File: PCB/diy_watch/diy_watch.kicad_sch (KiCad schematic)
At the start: 45 parts, among them J1 USB_B_Micro, SW1 SW_Push, U1 W25Q32JVSS, U2 DS3231MZ, U3 RP2040, U5 LTC4054ES5-4.2, U7 XC6210B332MR, Y1 12MHz_crystal

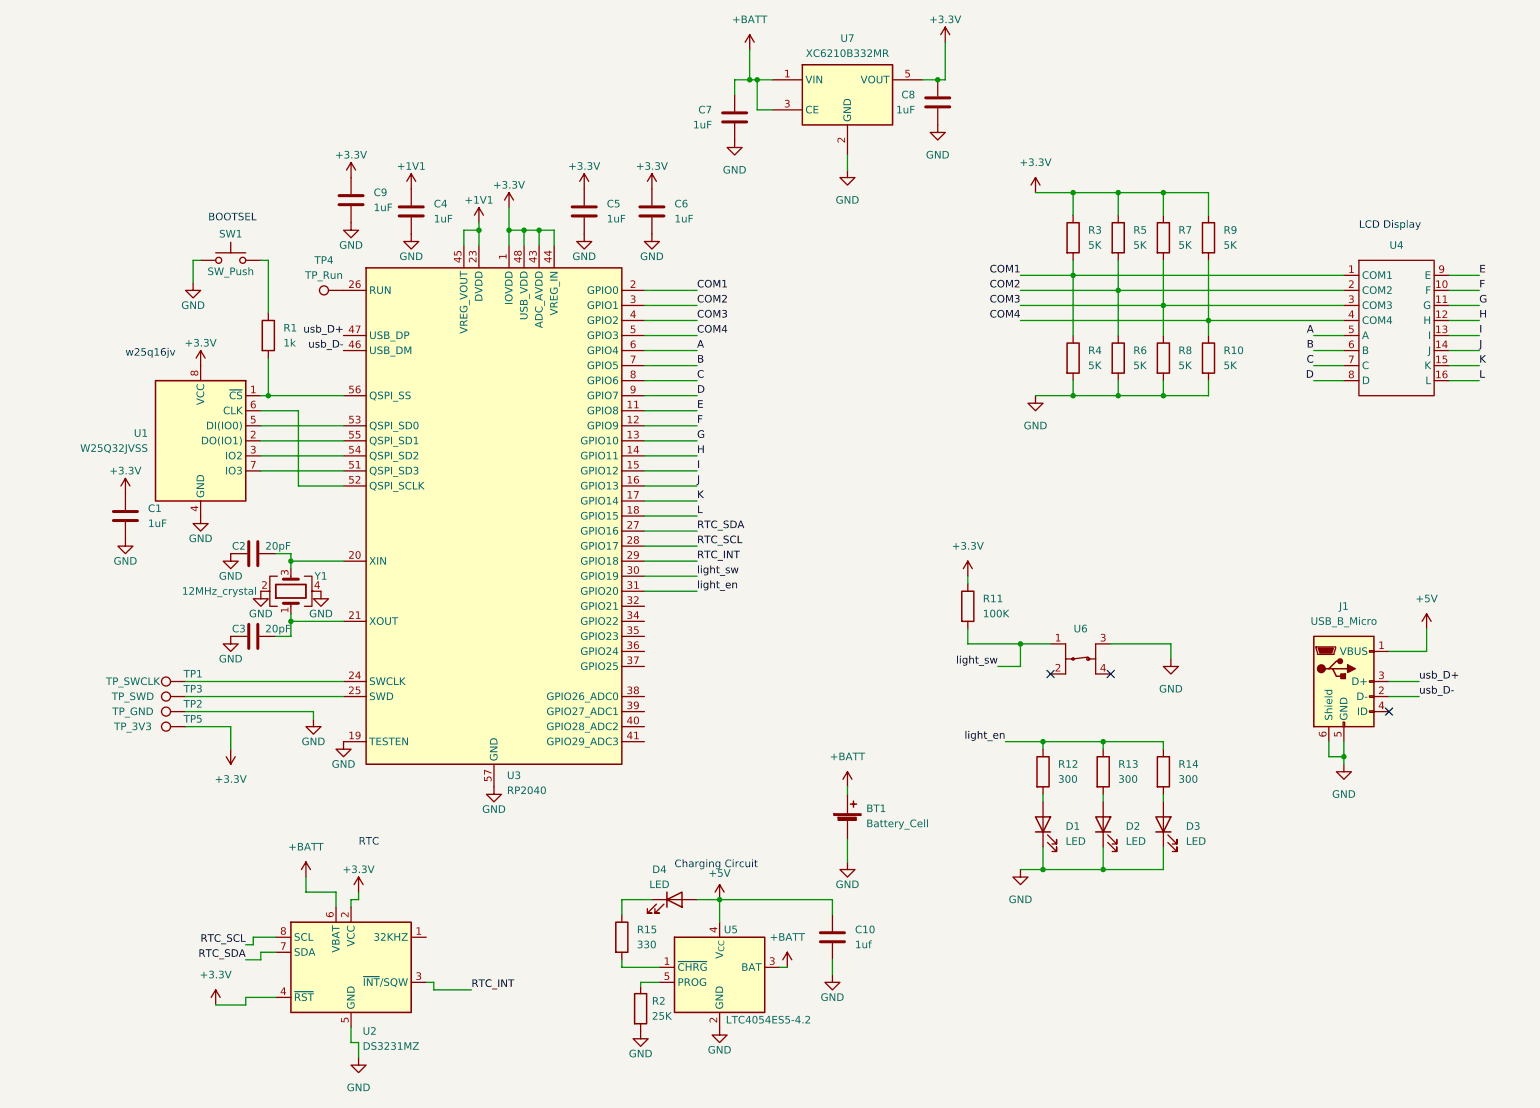
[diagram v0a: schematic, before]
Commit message: Changed charging chip and flash chip, rearranged parts
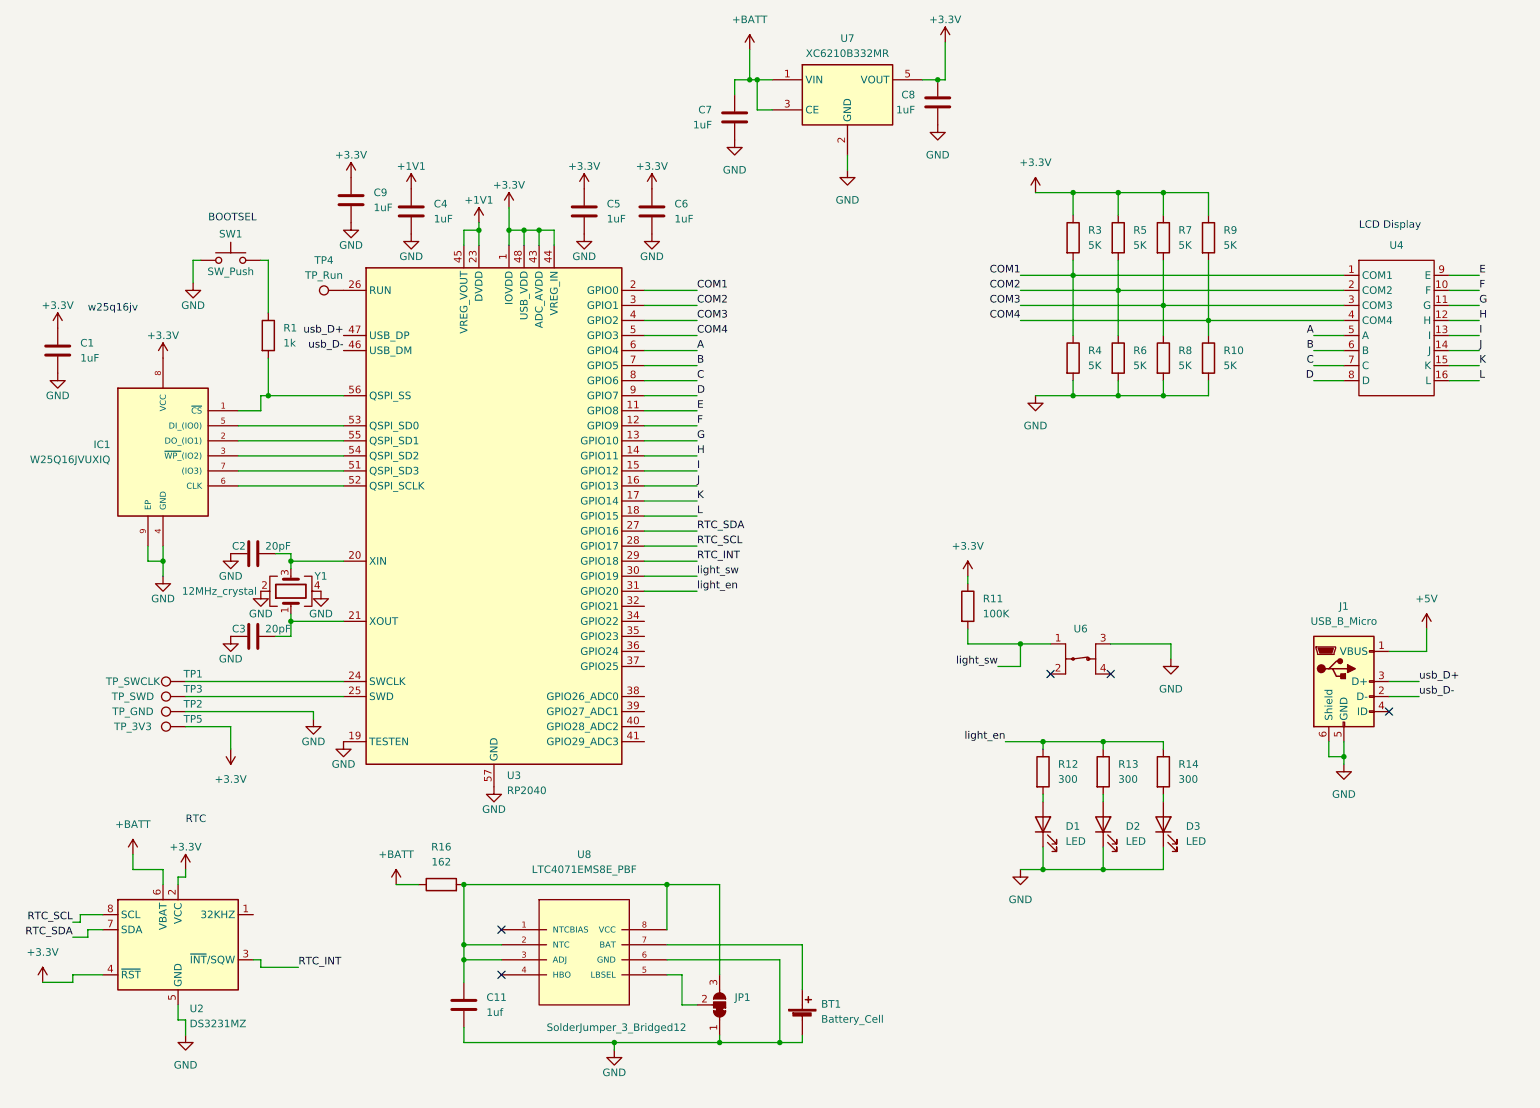
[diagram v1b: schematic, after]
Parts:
- removed C10: 1uf, Capacitor_SMD:C_0402_1005Metric, symbol Device:C
- removed D4: LED, LED_SMD:LED_0805_2012Metric_Pad1.15x1.40mm_HandSolder, symbol Device:LED
- removed R15: 330, Resistor_SMD:R_0805_2012Metric_Pad1.20x1.40mm_HandSolder, symbol Device:R
- removed R2: 25K, Resistor_SMD:R_0402_1005Metric, symbol Device:R
- removed U1: W25Q32JVSS, Package_SO:SOIC-8_3.9x4.9mm_P1.27mm, symbol Memory_Flash:W25Q32JVSS
- removed U5: LTC4054ES5-4.2, Package_TO_SOT_SMD:TSOT-23-5, symbol Battery_Management:LTC4054ES5-4.2
- added C11: 1uf, Capacitor_SMD:C_0402_1005Metric, symbol Device:C
- added IC1: W25Q16JVUXIQ, DIY_Watch_lib:SON50P300X200X60-9N, symbol DIY_Watch_lib:W25Q16JVUXIQ
- added JP1: SolderJumper_3_Bridged12, Jumper:SolderJumper-3_P1.3mm_Bridged12_Pad1.0x1.5mm, symbol Jumper:SolderJumper_3_Bridged12
- added R16: 162, Resistor_SMD:R_0402_1005Metric, symbol Device:R
- added U8: LTC4071EMS8E_PBF, Package_SO:MSOP-8-1EP_3x3mm_P0.65mm_EP1.5x1.8mm_ThermalVias, symbol DIY_Watch_lib:LTC4071EMS8E_PBF
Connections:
- net +3.3V: now also IC1.8 (VCC)
- net +BATT: now also R16.1; no longer BT1.1 (+)
- net GND: now also C11.2, IC1.4 (GND), IC1.9 (EP), JP1.1 (A), U8.6 (GND)
- net at R1.2, U3.56 (QSPI_SS): now also IC1.1 (~{CS})
- net at U3.55 (QSPI_SD1): now also IC1.2 (DO_(IO1))
- net at U3.54 (QSPI_SD2): now also IC1.3 (~{WP_}(IO2))
- net at U3.53 (QSPI_SD0): now also IC1.5 (DI_(IO0))
- net at U3.52 (QSPI_SCLK): now also IC1.6 (CLK)
- net at U3.51 (QSPI_SD3): now also IC1.7 ((IO3))
- new net: C11.1, JP1.3 (B), R16.2, U8.2 (NTC), U8.3 (ADJ), U8.8 (VCC)
- new net: JP1.2 (C), U8.5 (LBSEL)
- new net: BT1.1 (+), U8.7 (BAT)
- no-connect marks 3 -> 5
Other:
- note removed: "Charging Circuit"
- moved on the sheet: BT1, C1, U2

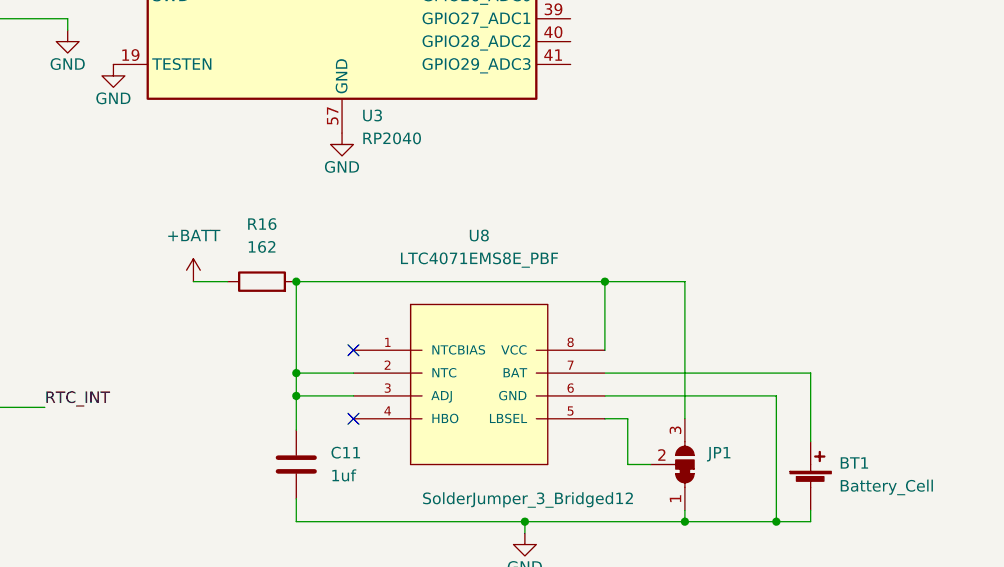
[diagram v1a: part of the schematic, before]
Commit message: Re-routed refactored board
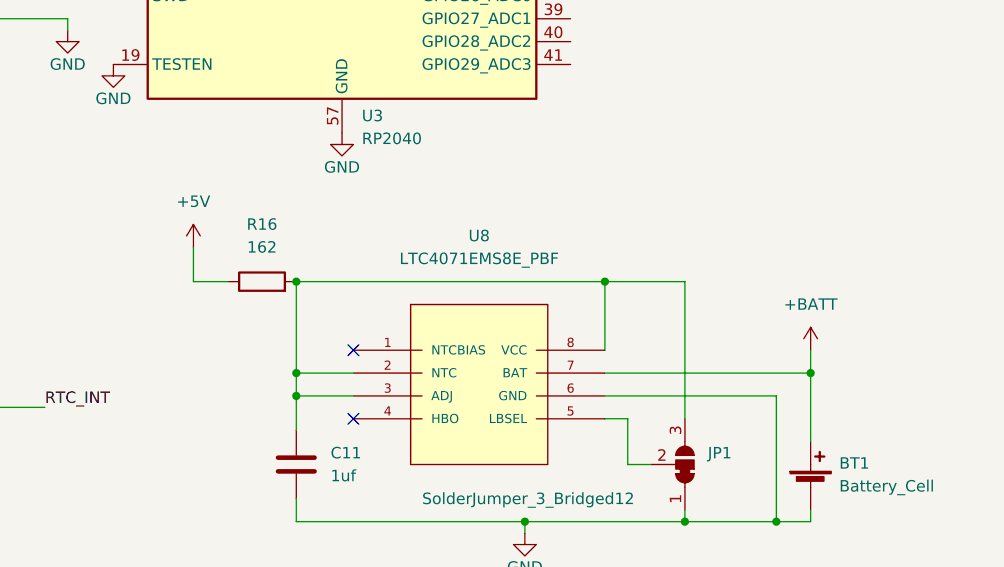
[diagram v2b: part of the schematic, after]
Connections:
- net +5V: now also R16.1
- net +BATT: now also BT1.1 (+), U8.7 (BAT); no longer R16.1
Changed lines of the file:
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@@
   (junction (at 195.58 158.75) (diameter 0) (color 0 0 0 0)
   )
+  (junction (at 154.94 171.45) (diameter 0) (color 0 0 0 0)
+  )
   (no_connect (at 207.01 125.73))
   (no_connect (at 104.14 168.91))
@@
     (stroke (width 0) (type default))
   )
-  (wire (pts (xy 154.94 171.45) (xy 154.94 179.07))
+  (wire (pts (xy 154.94 168.91) (xy 154.94 171.45))
     (stroke (width 0) (type default))
   )
@@
     (stroke (width 0) (type default))
   )
-  (wire (pts (xy 86.36 161.29) (xy 90.17 161.29))
-    (stroke (width 0) (type default))
-  )
   (wire (pts (xy 191.77 158.75) (xy 195.58 158.75))
     (stroke (width 0) (type default))
@@
     (stroke (width 0) (type default))
   )
+  (wire (pts (xy 154.94 171.45) (xy 154.94 179.07))
+    (stroke (width 0) (type default))
+  )
   (wire (pts (xy 110.49 50.8) (xy 110.49 53.34))
     (stroke (width 0) (type default))
@@
     (stroke (width 0) (type default))
   )
+  (wire (pts (xy 86.36 157.48) (xy 86.36 161.29))
+    (stroke (width 0) (type default))
+  )
   (wire (pts (xy 264.16 58.42) (xy 269.24 58.42))
     (stroke (width 0) (type default))
@@
     (stroke (width 0) (type default))
   )
+  (wire (pts (xy 86.36 161.29) (xy 90.17 161.29))
+    (stroke (width 0) (type default))
+  )
   (wire (pts (xy 241.3 73.66) (xy 246.38 73.66))
     (stroke (width 0) (type default))
@@
     )
   )
+  (symbol (lib_id "power:+5V") (at 86.36 157.48 0) (unit 1)
+    (in_bom yes) (on_board yes) (dnp no) (fields_autoplaced)
+    (property "Reference" "#PWR021" (at 86.36 161.29 0)
+      (effects (font (size 1.27 1.27)) hide)
+    )
+    (property "Value" "+5V" (at 86.36 152.4 0)
+      (effects (font (size 1.27 1.27)))
+    )
+    (property "Footprint" "" (at 86.36 157.48 0)
+      (effects (font (size 1.27 1.27)) hide)
+    )
+    (property "Datasheet" "" (at 86.36 157.48 0)
+      (effects (font (size 1.27 1.27)) hide)
+    )
+    (pin "1")
+    (instances
+      (project "diy_watch"
+        (path "/12c7509a-2a16-4dc7-8785-00872e5a9f11"
+          (reference "#PWR021") (unit 1)
+        )
+      )
+    )
+  )
   (symbol (lib_id "power:GND") (at 162.56 40.64 0) (unit 1)
     (in_bom yes) (on_board yes) (dnp no) (fields_autoplaced)
@@
     )
   )
-  (symbol (lib_id "power:+BATT") (at 86.36 161.29 0) (unit 1)
+  (symbol (lib_id "power:+BATT") (at 154.94 168.91 0) (unit 1)
     (in_bom yes) (on_board yes) (dnp no)
-    (property "Reference" "#PWR025" (at 86.36 165.1 0)
+    (property "Reference" "#PWR025" (at 154.94 172.72 0)
       (effects (font (size 1.27 1.27)) hide)
     )
-    (property "Value" "+BATT" (at 86.36 156.21 0)
+    (property "Value" "+BATT" (at 154.94 163.83 0)
       (effects (font (size 1.27 1.27)))
     )
-    (property "Footprint" "" (at 86.36 161.29 0)
+    (property "Footprint" "" (at 154.94 168.91 0)
       (effects (font (size 1.27 1.27)) hide)
     )
-    (property "Datasheet" "" (at 86.36 161.29 0)
+    (property "Datasheet" "" (at 154.94 168.91 0)
       (effects (font (size 1.27 1.27)) hide)
     )

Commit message: Fixing DRC errors on PCB
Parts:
- U8: footprint Package_SO:MSOP-8-1EP_3x3mm_P0.65mm_EP1.5x1.8mm_ThermalVias -> Package_SO:MSOP-8-1EP_3x3mm_P0.65mm_EP1.5x1.8mm
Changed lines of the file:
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@@
       (effects (font (size 1.27 1.27)))
     )
-    (property "Footprint" "Package_SO:MSOP-8-1EP_3x3mm_P0.65mm_EP1.5x1.8mm_ThermalVias" (at 76.2 146.05 0)
+    (property "Footprint" "Package_SO:MSOP-8-1EP_3x3mm_P0.65mm_EP1.5x1.8mm" (at 76.2 146.05 0)
       (effects (font (size 1.27 1.27)) (justify bottom) hide)
     )

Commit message: Adding BOM
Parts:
- R12: footprint LED_SMD:LED_0402_1005Metric -> Resistor_SMD:R_0402_1005Metric
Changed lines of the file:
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@@
       (effects (font (size 1.27 1.27)) (justify left))
     )
-    (property "Footprint" "LED_SMD:LED_0402_1005Metric" (at 193.802 142.24 90)
+    (property "Footprint" "Resistor_SMD:R_0402_1005Metric" (at 193.802 142.24 90)
       (effects (font (size 1.27 1.27)) hide)
     )

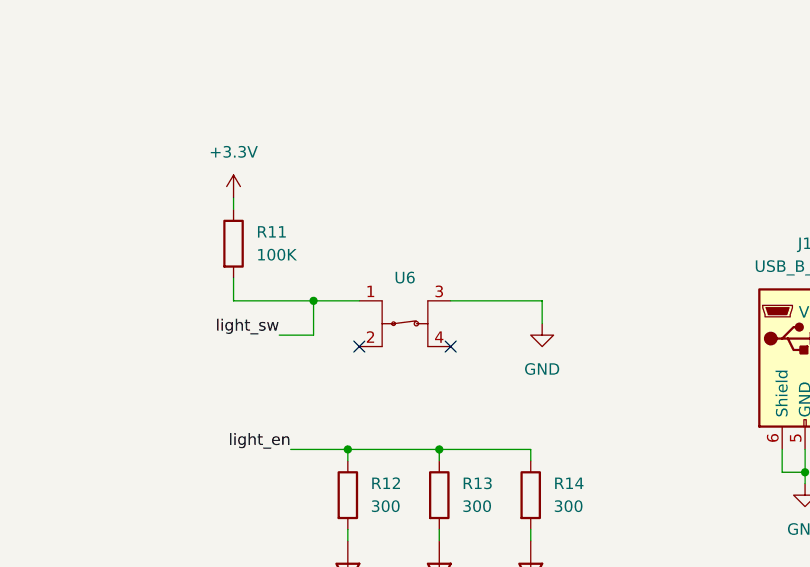
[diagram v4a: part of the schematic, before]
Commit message: Updating components for stock reasons
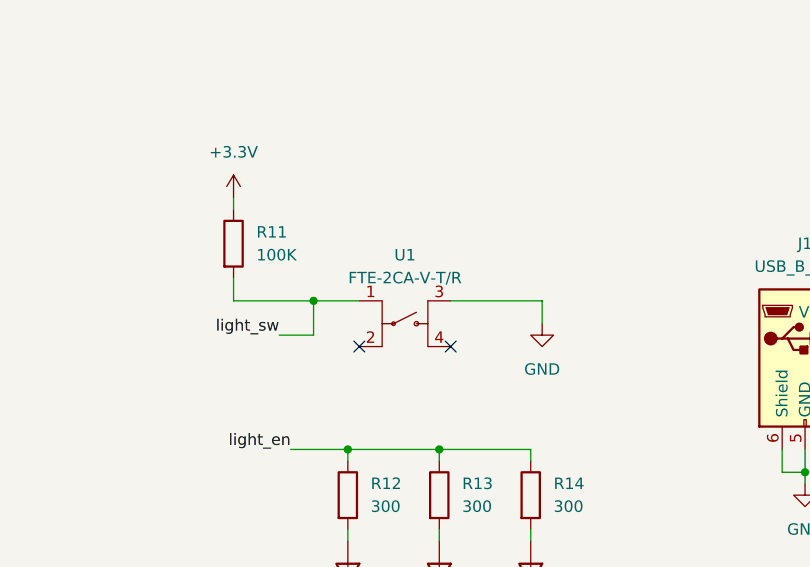
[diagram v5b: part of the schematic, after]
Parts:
- removed U6: ~, DIY_Watch_lib:Diptronics FTE-3, symbol DIY_Watch_lib:Diptronics_FTE-3CA-V-T/R
- added U1: FTE-2CA-V-T/R, DIY_Watch_lib:Diptronics FTE-3, symbol DIY_Watch_lib:FTE-2CA-V-T/R
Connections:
- net GND: now also U1.3
- net light_sw: now also U1.1
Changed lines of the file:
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@@
+    )
+  )
+  (symbol (lib_id "DIY_Watch_lib:FTE-2CA-V-T/R") (at 201.93 121.92 0) (unit 1)
+    (in_bom yes) (on_board yes) (dnp no) (fields_autoplaced)
+    (property "Reference" "U1" (at 201.93 115.57 0)
+      (effects (font (size 1.27 1.27)))
+    )
+    (property "Value" "FTE-2CA-V-T/R" (at 201.93 118.11 0)
+      (effects (font (size 1.27 1.27)))
+    )
+    (property "Footprint" "DIY_Watch_lib:Diptronics FTE-3" (at 201.93 121.92 0)
+      (effects (font (size 1.27 1.27)) hide)
+    )
+    (property "Datasheet" "" (at 201.93 121.92 0)
+      (effects (font (size 1.27 1.27)) hide)
+    )
+    (pin "1")
+    (pin "2")
+    (pin "3")
+    (pin "4")
+    (instances
+      (project "diy_watch"
+        (path "/12c7509a-2a16-4dc7-8785-00872e5a9f11"
+          (reference "U1") (unit 1)
+        )
+      )
     )
   )
@@
         )
       )
-    )
-  )
-  (symbol (lib_id "DIY_Watch_lib:Diptronics_FTE-3CA-V-T/R") (at 201.93 121.92 0) (unit 1)
-    (in_bom yes) (on_board yes) (dnp no) (fields_autoplaced)
-    (property "Reference" "U6" (at 201.93 118.11 0)
-      (effects (font (size 1.27 1.27)))
-    )
-    (property "Value" "~" (at 201.93 121.92 0)
-      (effects (font (size 1.27 1.27)))
-    )
-    (property "Footprint" "DIY_Watch_lib:Diptronics FTE-3" (at 201.93 121.92 0)
-      (effects (font (size 1.27 1.27)) hide)
-    )
-    (property "Datasheet" "" (at 201.93 121.92 0)
-      (effects (font (size 1.27 1.27)) hide)
-    )
-    (pin "1")
-    (pin "2")
-    (pin "3")
-    (pin "4")
-    (instances
-      (project "diy_watch"
-        (path "/12c7509a-2a16-4dc7-8785-00872e5a9f11"
-          (reference "U6") (unit 1)
-        )
-      )

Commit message: Adding fixes to PCB schematic
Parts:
- added R15, R17, R2: 10K, Resistor_SMD:R_0402_1005Metric, symbol Device:R
- added R18, R19: 27R, Resistor_SMD:R_0402_1005Metric, symbol Device:R
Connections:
- net +3.3V: now also R15.1, R17.1, R2.1
- net +BATT: no longer C7.1, U7.1 (VIN), U7.3 (CE)
- net RTC_INT: now also R17.2
- net RTC_SCL: now also R15.2
- net RTC_SDA: now also R2.2
- net usb_D+: now also R19.1; no longer U3.47 (USB_DP)
- net usb_D-: now also R18.1; no longer U3.46 (USB_DM)
- net VCC: now reaches C11.1, JP1.3 (B), R16.2, U8.2 (NTC), U8.3 (ADJ), U8.8 (VCC)
- net VCC: now also C7.1, U7.1 (VIN), U7.3 (CE)
- new net USB_DMX: R18.2, U3.46 (USB_DM)
- new net USB_DPX: R19.2, U3.47 (USB_DP)
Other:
- moved on the sheet: R1, SW1
